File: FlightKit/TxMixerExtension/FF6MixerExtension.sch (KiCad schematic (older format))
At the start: 26 parts, among them K1 CONN_3, K2 CONN_3, K3 CONN_3, K4 CONN_3, P1 CONN_4, P2 CONN_6, P3 CONN_8, P4 CONN_4, Q1 MOS_N, Q2 MOS_N, Q3 MOS_N, Q4 MOS_N

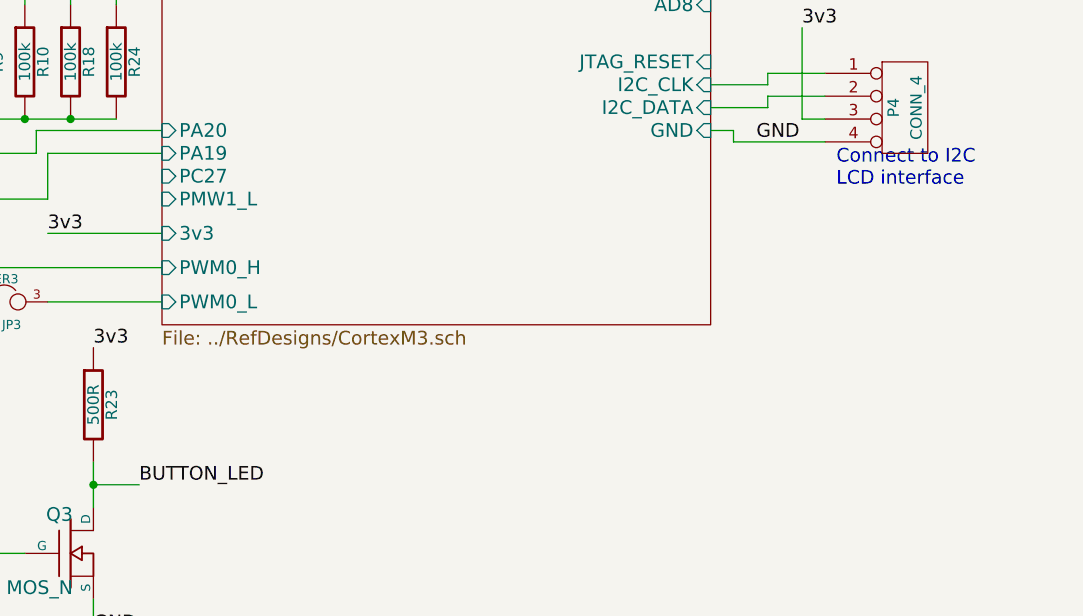
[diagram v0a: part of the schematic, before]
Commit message: Added speaker and updated module list
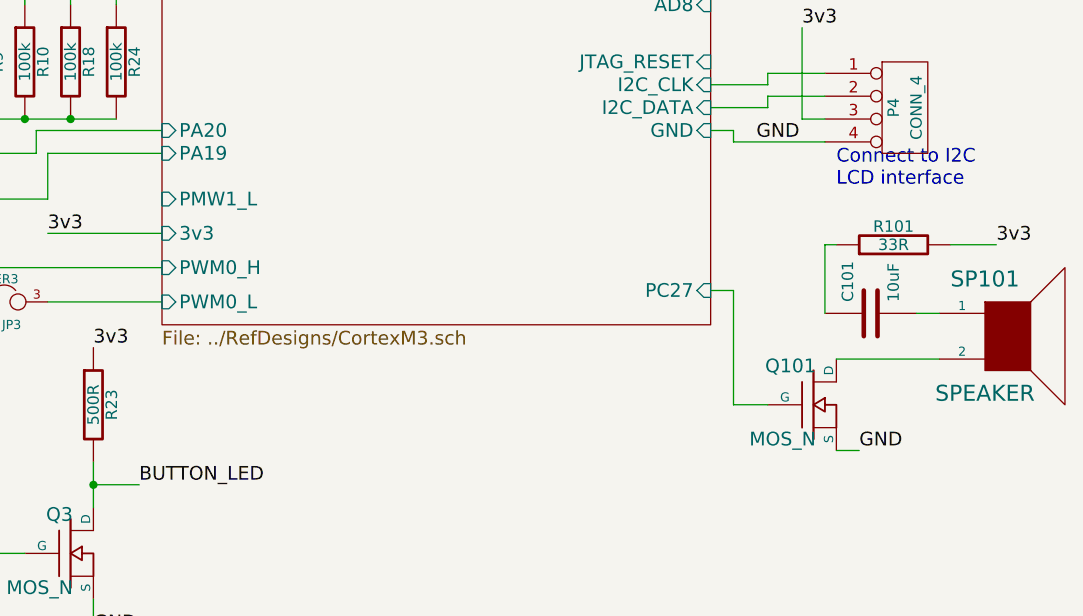
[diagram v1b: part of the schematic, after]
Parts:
- added C101: 10uF, symbol C
- added Q101: MOS_N, symbol MOS_N
- added R101: 33R, symbol R
- added SP101: SPEAKER, symbol SPEAKER
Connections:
- net 3v3: now also R101.2
- net ARM Cortex M3/PC27: now also Q101.G
- net GND: now also Q101.S
- new net: Q101.D, SP101.2
- new net: C101.1, R101.1
- new net: C101.2, SP101.1
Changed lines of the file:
@@
-EESchema Schematic File Version 2  date Tue 30 Jul 2013 15:21:28 BST
+EESchema Schematic File Version 2  date Wed 31 Jul 2013 19:40:22 BST
 LIBS:power
 LIBS:device
@@
 Sheet 1 3
 Title ""
-Date "30 jul 2013"
+Date "31 jul 2013"
 Rev ""
 Comp ""
@@
 Comment4 ""
 $EndDescr
-Text Label 6750 6450 0    60   ~ 0
-3v3
+Wire Wire Line
+	10000 6900 10100 6900
+Wire Wire Line
+	10350 6300 10450 6300
+Wire Wire Line
+	10500 6000 10700 6000
 Wire Wire Line
 	7050 4850 5650 4850
@@
 Wire Wire Line
 	5650 4650 7050 4650
+Wire Wire Line
+	9450 6200 9550 6200
+Wire Wire Line
+	9550 6200 9550 6700
+Wire Wire Line
+	9550 6700 9700 6700
+Wire Wire Line
+	10000 6000 9950 6000
+Wire Wire Line
+	9950 6000 9950 6300
+Wire Wire Line
+	10450 6500 10000 6500
+Text Label 10100 6900 0    60   ~ 0
+GND
+$Comp
+L C C101
+U 1 1 51F95952
+P 10150 6300
+F 0 "C101" H 10200 6400 50  0000 L CNN
+F 1 "10uF" H 10200 6200 50  0000 L CNN
+	1    10150 6300
+	0    -1   -1   0
+$EndComp
+Text Label 10700 6000 0    60   ~ 0
+3v3
+$Comp
+L SPEAKER SP101
+U 1 1 51F9593D
+P 10750 6400
+F 0 "SP101" H 10650 6650 70  0000 C CNN
+F 1 "SPEAKER" H 10650 6150 70  0000 C CNN
+	1    10750 6400
+	1    0    0    -1
+$EndComp
+$Comp
+L R R101
+U 1 1 51F9592B
+P 10250 6000
+F 0 "R101" V 10330 6000 50  0000 C CNN
+F 1 "33R" V 10250 6000 50  0000 C CNN
+	1    10250 6000
+	0    -1   -1   0
+$EndComp
+$Comp
+L MOS_N Q101
+U 1 1 51F9590E
+P 9900 6700
+F 0 "Q101" H 9910 6870 60  0000 R CNN
+F 1 "MOS_N" H 9910 6550 60  0000 R CNN
+	1    9900 6700
+	1    0    0    -1
+$EndComp
+Text Label 6750 6450 0    60   ~ 0
+3v3
 Text Label 5750 5700 0    60   ~ 0
 GND
@@
 F19 "PWM0_H" I L 7050 6100 60
 F20 "PWM0_L" I L 7050 6250 60
-F21 "PC27" I L 7050 5700 60
+F21 "PC27" I R 9450 6200 60
 F22 "PWM3_H" I R 9450 2500 60
 F23 "PWM3_L" I R 9450 2650 60

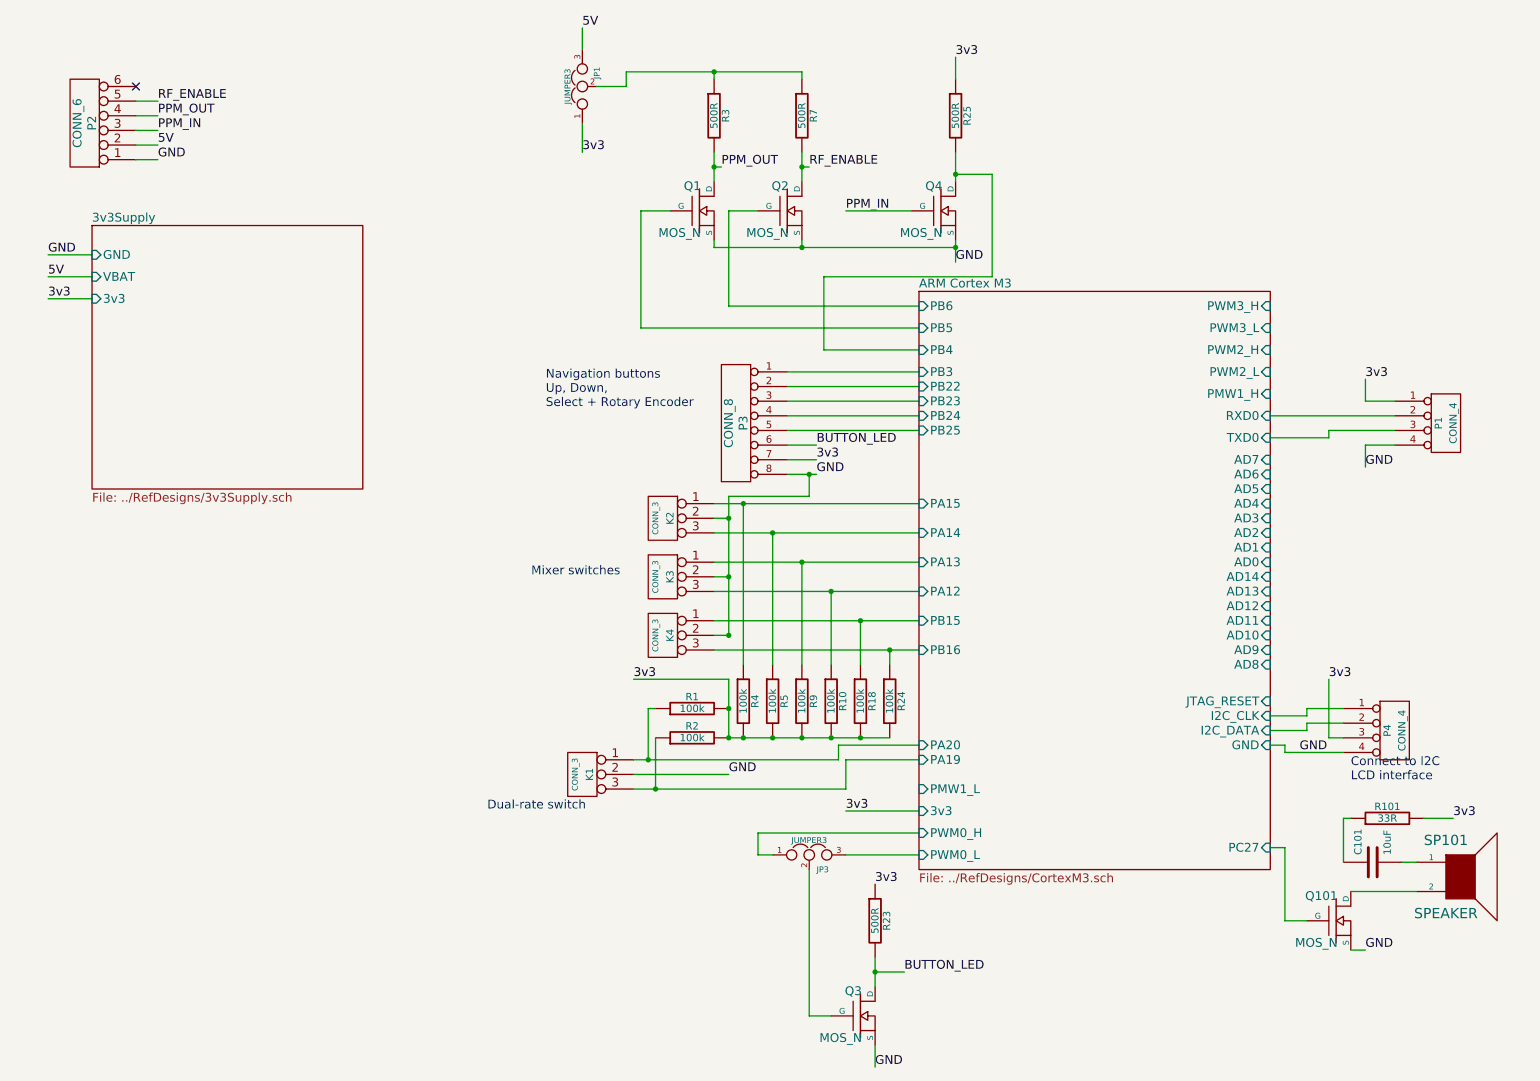
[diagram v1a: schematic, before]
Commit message: Added speaker type and supplier
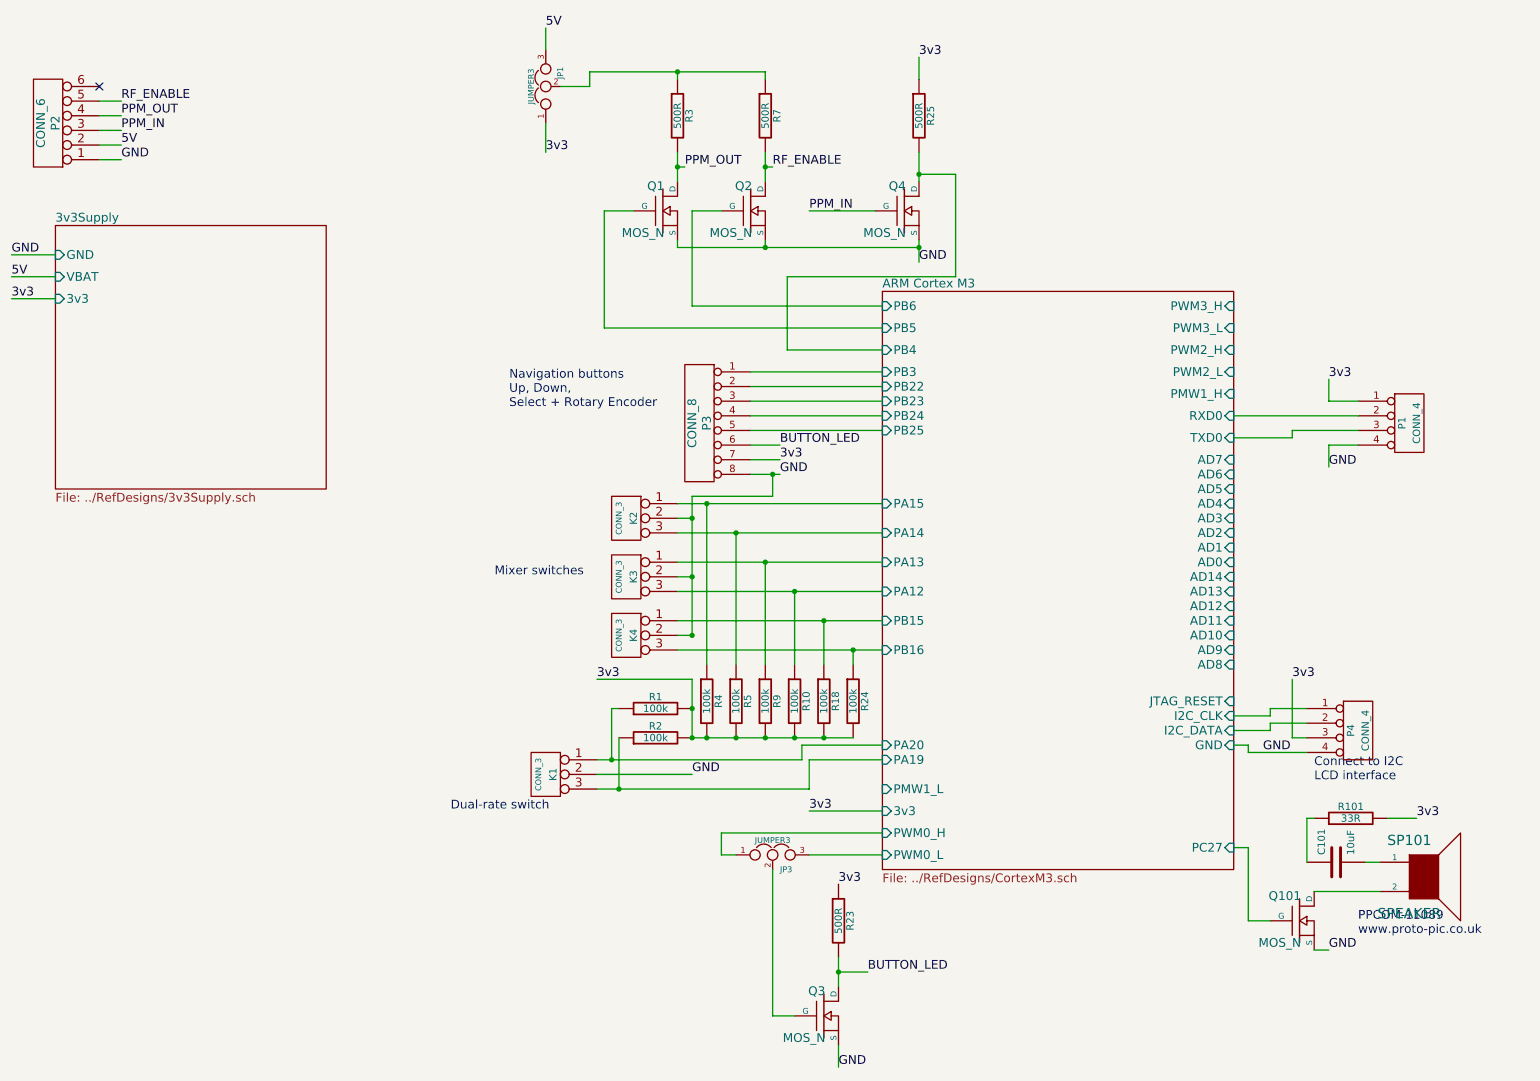
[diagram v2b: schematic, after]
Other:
- note added: "PPCOM-11089\nwww.proto-pic.co.uk"
- moved on the sheet: C101, JP1, JP3, K1, K2, K3, K4, P1, P2, P3, P4, Q1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
